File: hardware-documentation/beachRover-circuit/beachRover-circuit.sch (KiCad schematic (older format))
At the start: 4 parts

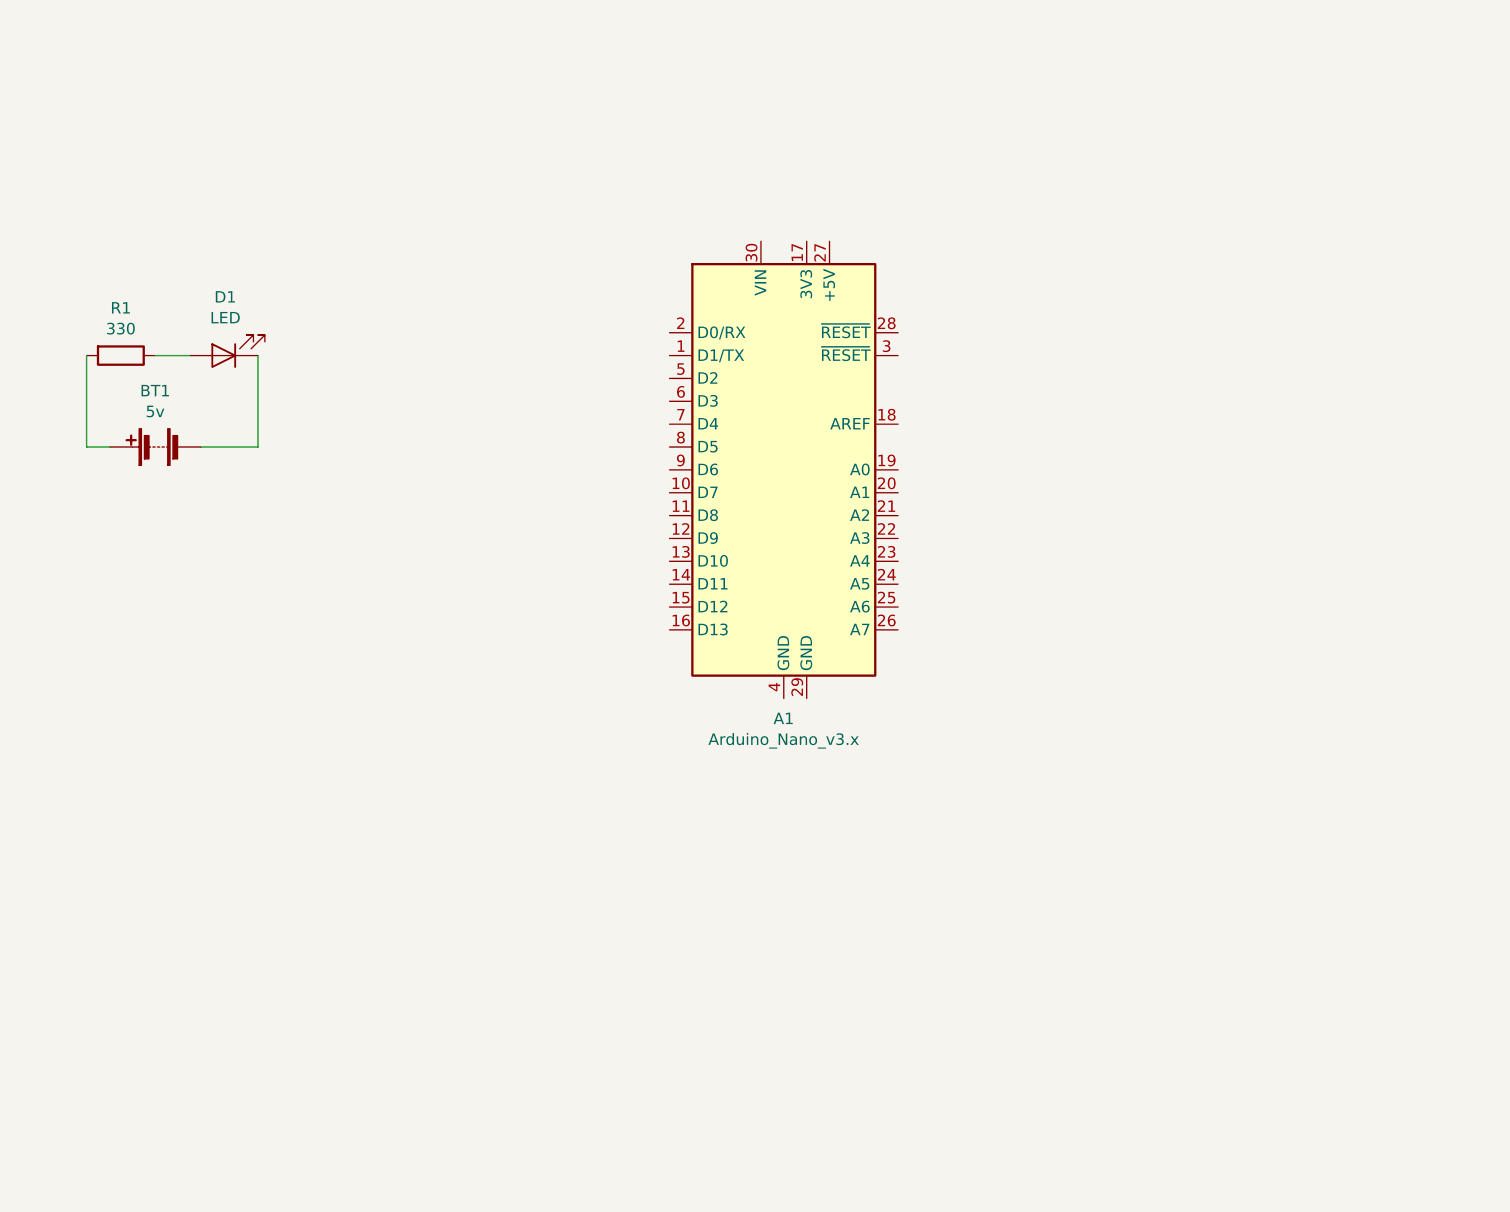
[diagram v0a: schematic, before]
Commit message: Added few components in schematic and assigned footprints
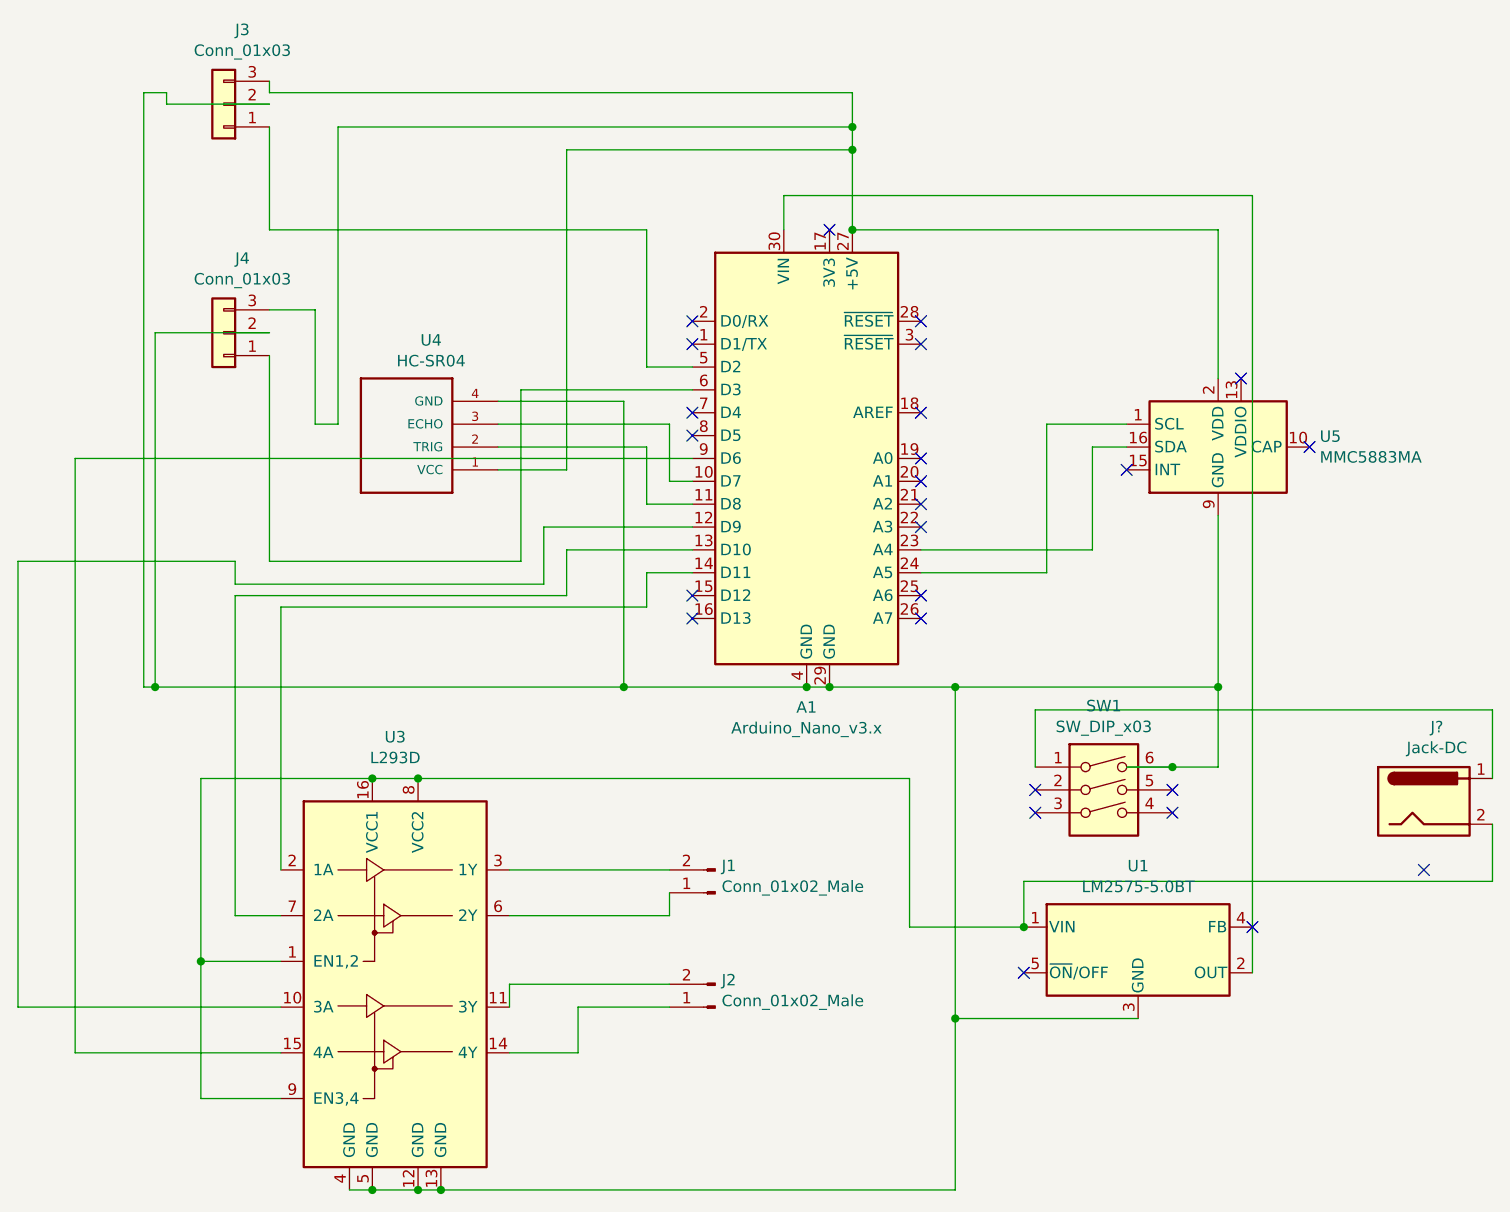
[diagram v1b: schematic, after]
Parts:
- removed BT1: 5v, Battery:BatteryHolder_TruPower_BH-331P_3xAA, symbol Device:Battery
- removed D1: LED, LED_THT:LED_D5.0mm, symbol Device:LED
- removed R1: 330, Resistor_THT:R_Axial_DIN0411_L9.9mm_D3.6mm_P15.24mm_Horizontal, symbol Device:R
- added J1, J2: Conn_01x02_Male, Connector_PinHeader_2.54mm:PinHeader_1x02_P2.54mm_Vertical, symbol Connector:Conn_01x02_Male
- added J3, J4: Conn_01x03, Connector_PinSocket_2.54mm:PinSocket_1x03_P2.54mm_Vertical, symbol Connector_Generic:Conn_01x03
- added J?: Jack-DC, symbol Connector:Jack-DC
- added SW1: SW_DIP_x03, Button_Switch_THT:SW_E-Switch_EG1271_DPDT, symbol Switch:SW_DIP_x03
- added U1: LM2575-5.0BT, Package_TO_SOT_THT:TO-220-5_Vertical, symbol Regulator_Switching:LM2575-5.0BT
- added U3: L293D, Package_DIP:DIP-16_W7.62mm, symbol Driver_Motor:L293D
- added U4: HC-SR04, HC-SR04:XCVR_HC-SR04, symbol HC-SR04:HC-SR04
- added U5: MMC5883MA, Package_LGA:LGA-16_3x3mm_P0.5mm, symbol Sensor_Magnetic:MMC5883MA
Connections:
- net at A1.10 (D7): now also U4.3 (ECHO)
- net at A1.11 (D8): now also U4.2 (TRIG)
- net at A1.12 (D9): now also U3.10 (3A)
- net at A1.13 (D10): now also U3.7 (2A)
- net at A1.14 (D11): now also U3.2 (1A)
- net at A1.23 (A4): now also U5.16 (SDA)
- net at A1.24 (A5): now also U5.1 (SCL)
- net at A1.27 (+5V): now also J3.3 (Pin_3), J4.3 (Pin_3), U4.1 (VCC), U5.2 (VDD)
- net at A1.29 (GND): now also A1.4 (GND), J3.2 (Pin_2), J4.2 (Pin_2), SW1.6, U1.3 (GND), U3.12 (GND), U3.13 (GND), U3.4 (GND), U3.5 (GND), U4.4 (GND), U5.11 (GND), U5.9 (GND)
- net at A1.30 (VIN): now also U1.2 (OUT)
- net at A1.5 (D2): now also J3.1 (Pin_1)
- net at A1.6 (D3): now also J4.1 (Pin_1)
- net at A1.9 (D6): now also U3.15 (4A)
- new net: J?.2, U1.1 (VIN), U3.1 (EN1,2), U3.16 (VCC1), U3.8 (VCC2), U3.9 (EN3,4)
- new net: J2.2 (Pin_2), U3.11 (3Y)
- new net: J2.1 (Pin_1), U3.14 (4Y)
- new net: J1.2 (Pin_2), U3.3 (1Y)
- new net: J1.1 (Pin_1), U3.6 (2Y)
- new net: J?.1, SW1.1
- no-connect marks 0 -> 26
